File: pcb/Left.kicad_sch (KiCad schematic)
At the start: 31 parts, among them J1 VIK_OUT_PMWL, J2 VIK_OUT_INTC, J5 Conn_01x02, U1 nice_nano, U3 MCP23017_SO

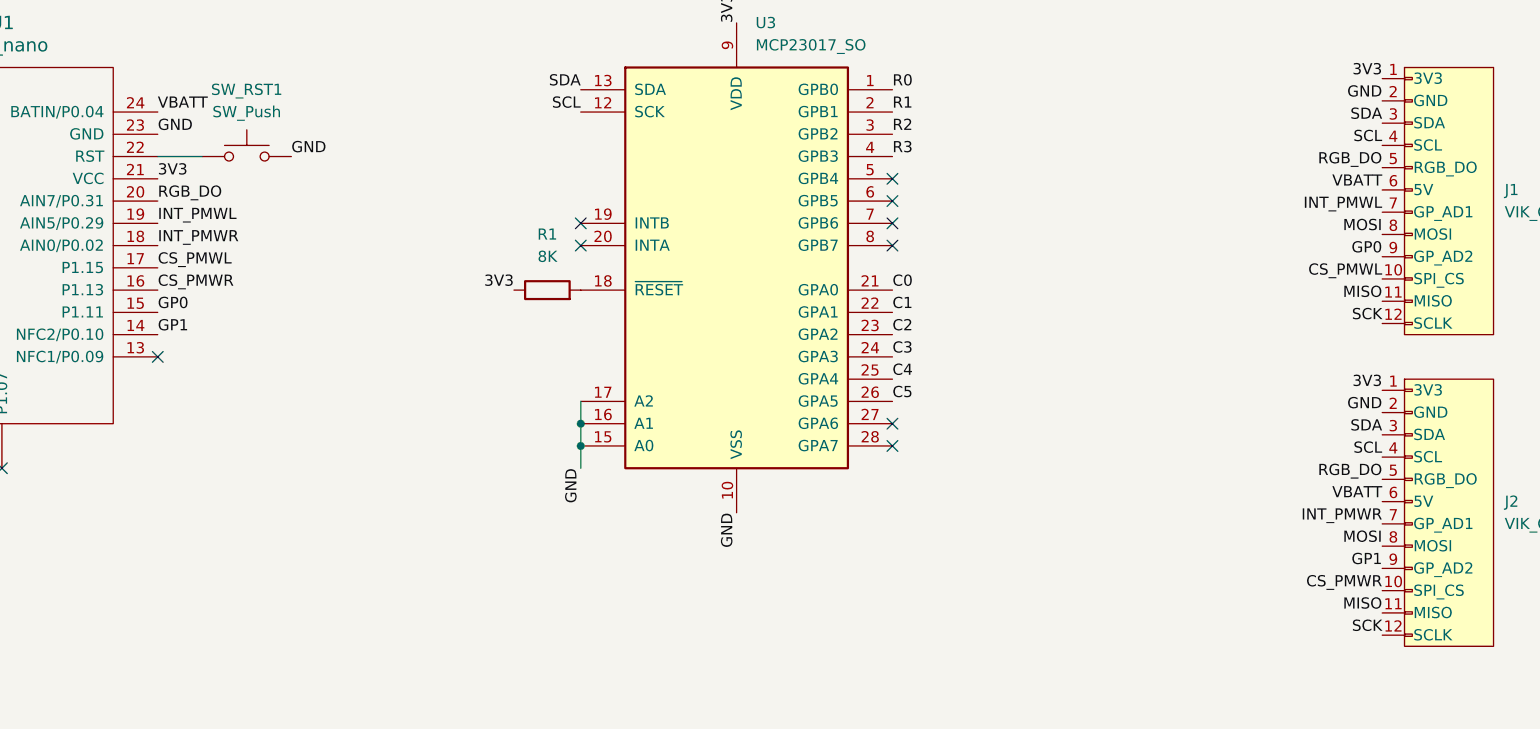
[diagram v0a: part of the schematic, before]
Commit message: Create VIK hat for Seeed Xiao nRF.
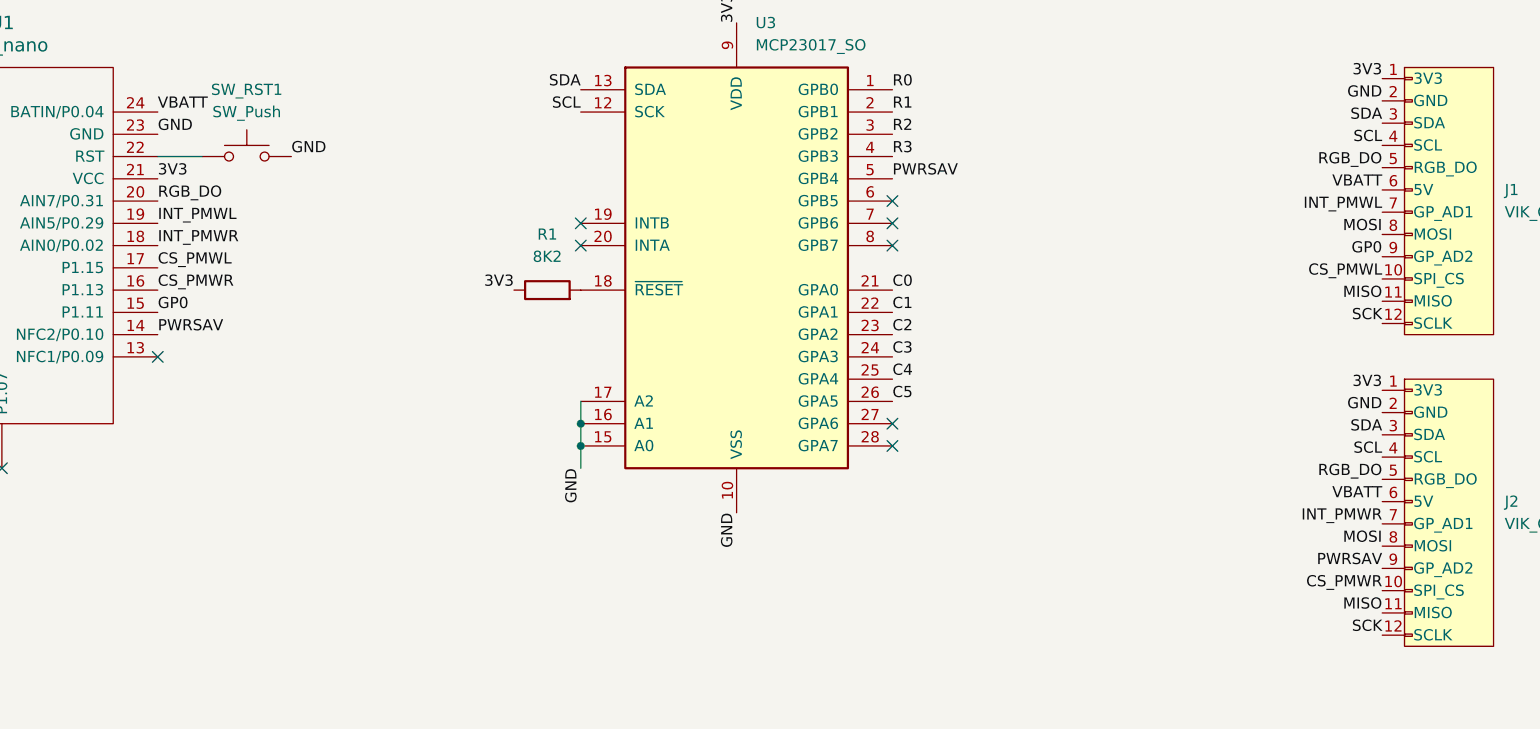
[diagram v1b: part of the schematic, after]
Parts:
- R1: value 8K -> 8K2
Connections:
- net GP1 is gone; now on net PWRSAV: J2.9 (GP_AD2), U1.14 (NFC2/P0.10)
- net PWRSAV: now reaches U3.5 (GPB4)
- no-connect marks 17 -> 16
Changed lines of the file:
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@@
 	)
 	(no_connect
-		(at 151.13 31.75)
-	)
-	(no_connect
 		(at 31.75 49.53)
 	)
@@
 		)
 	)
-	(label "GP1"
+	(label "PWRSAV"
 		(at 67.31 49.53 0)
 		(effects
@@
 		)
 	)
-	(label "GP1"
+	(label "PWRSAV"
 		(at 207.01 76.2 180)
 		(effects
@@
 		)
 	)
+	(label "PWRSAV"
+		(at 151.13 31.75 0)
+		(effects
+			(font
+				(size 1.27 1.27)
+			)
+			(justify left bottom)
+		)
+	)
 	(label "MISO"
 		(at 31.75 36.83 180)
@@
 			)
 		)
-		(property "Value" "8K"
+		(property "Value" "8K2"
 			(at 111.76 40.64 90)
 			(effects
